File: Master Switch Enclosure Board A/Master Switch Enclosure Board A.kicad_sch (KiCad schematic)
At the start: 22 parts, among them J1 DRC Connector, J10 2-pin Microfit, J11 2-pin Microfit, J12 1-pin Microfit, J13 2-pin Microfit, J2 DTM Connector, J3 XT90, J4 XT90, J5 Screw_Terminal_01x05, J5 XT90, J6 XT90, J7 2-pin Microfit, J8 4-pin Microfit, J9 2-pin Microfit, J9 DB9_Female

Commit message: schematics ready for review
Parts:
- J2: value DTM Connector -> Ribbon Connector
- JP1: footprint (none) -> Jumper:SolderJumper-2_P1.3mm_Open_RoundedPad1.0x1.5mm
- renumbered D1 to D11, J5 to J14, J9 to J15, R1 to R11, R2 to R12, R3 to R13, R4 to R14
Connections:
- net CANH_e is gone; now on net CANH_EM: J8.4 (Pin_4)
- net CANL_e is gone; now on net CANL_EM: J8.3 (Pin_3)
- net VCU_out is gone; now on net VCUWake_out: J11.2 (Pin_2)
- net GND: now also J2.20 (Pin_20)
- no-connect marks 8 -> 7

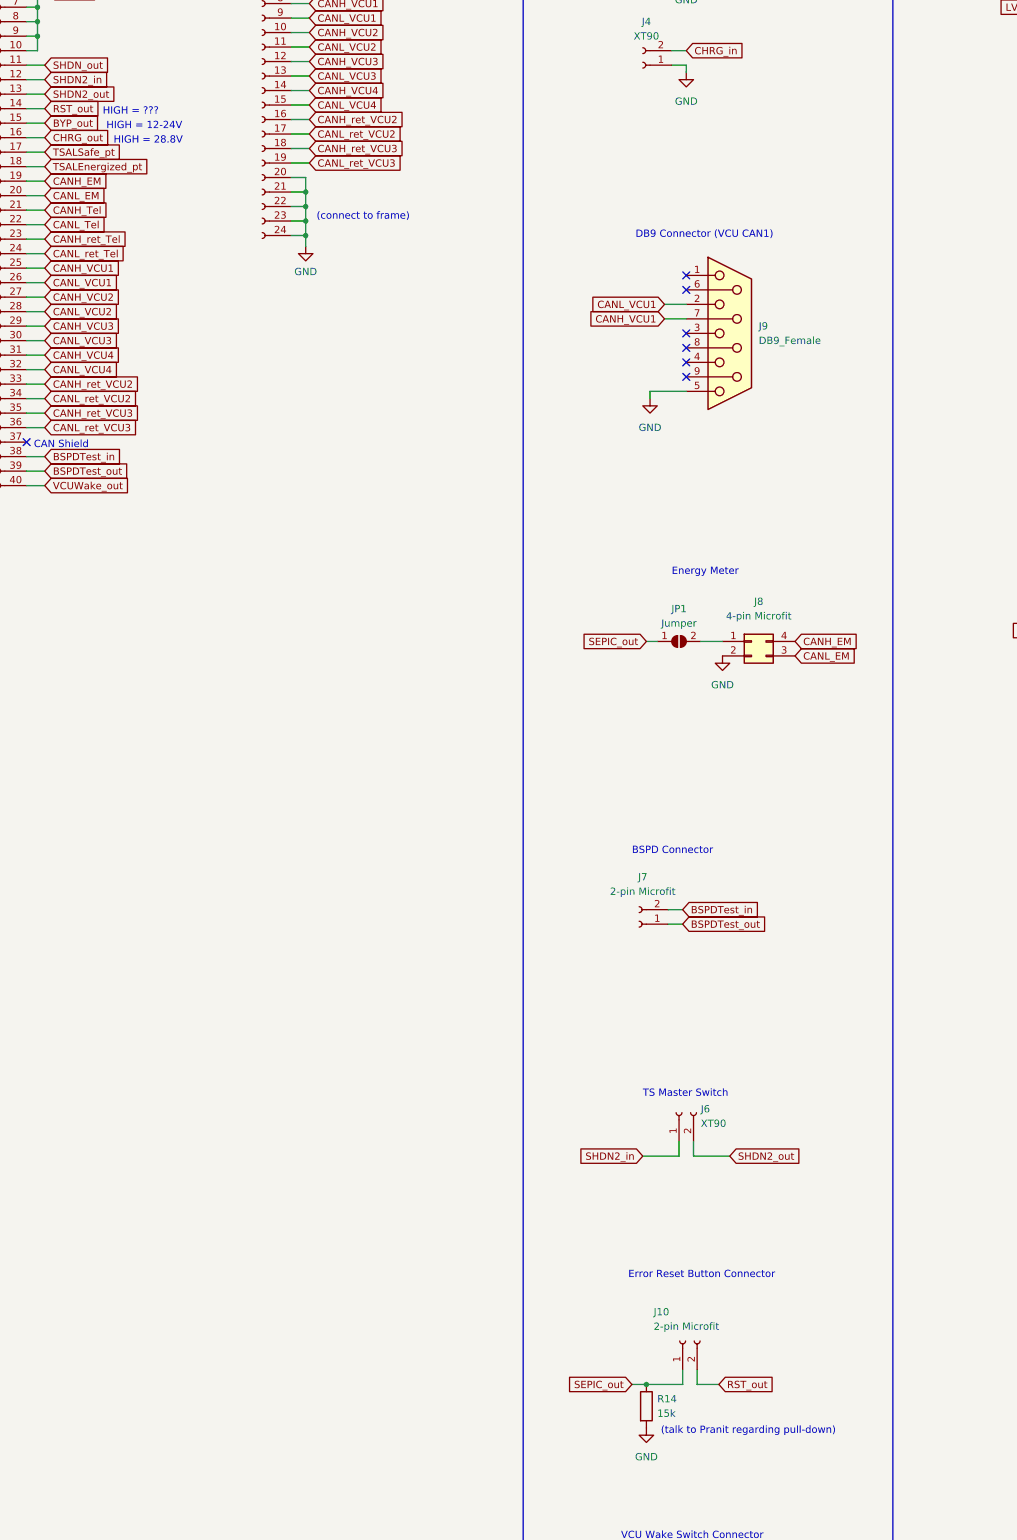
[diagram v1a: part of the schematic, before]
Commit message: resolved error reset requirements
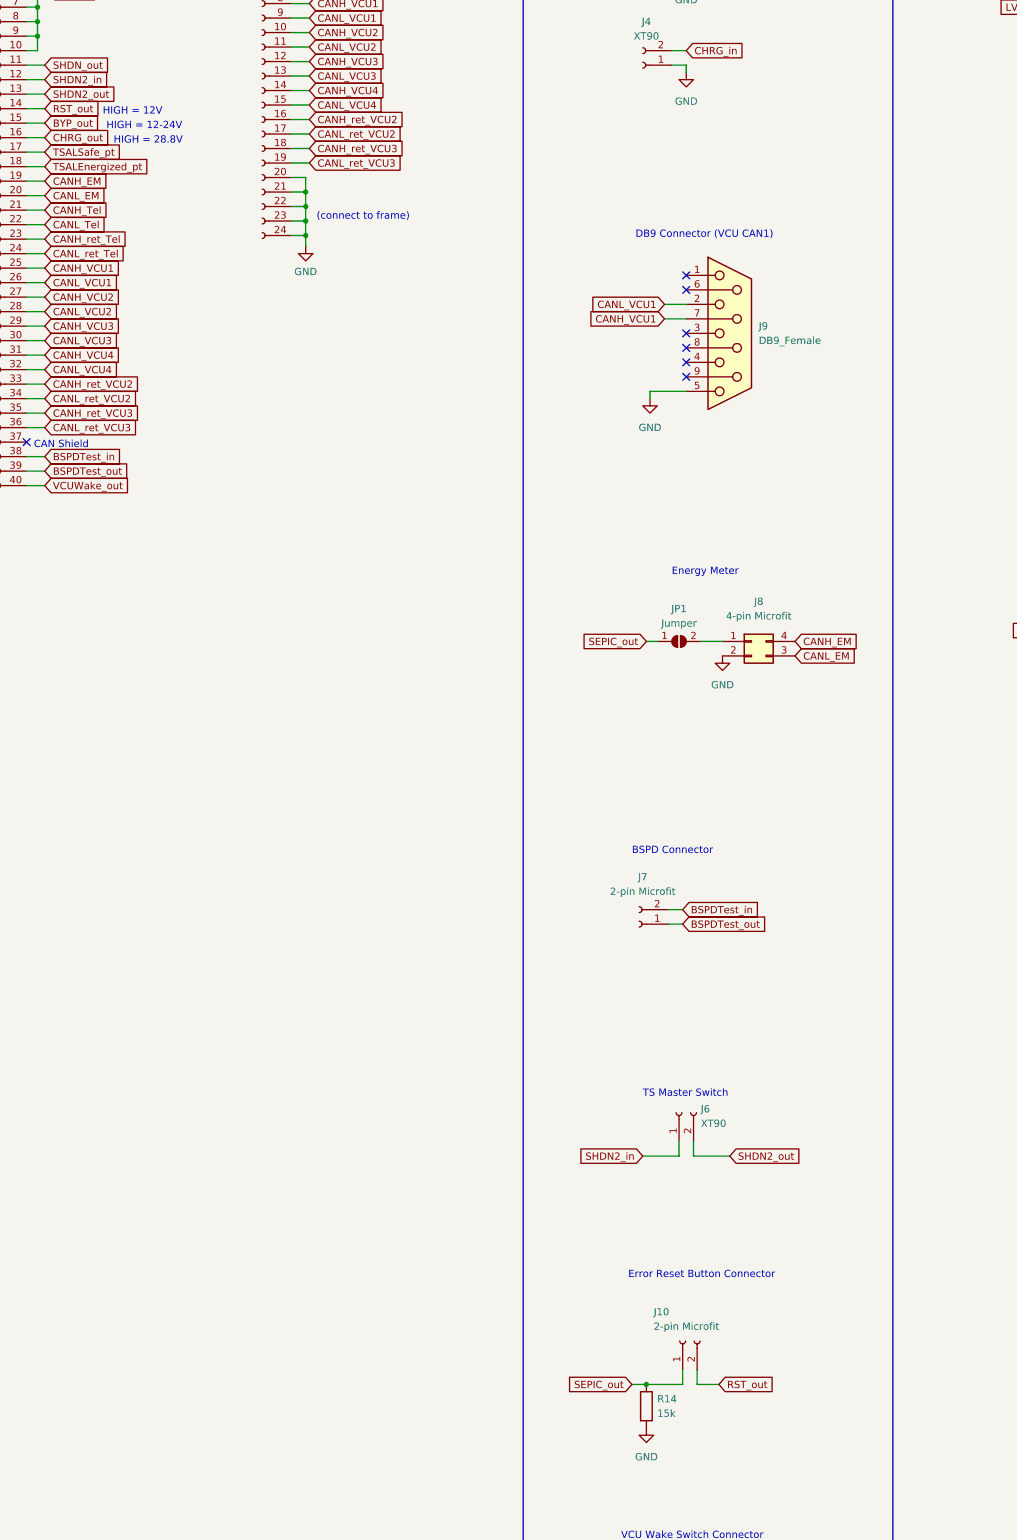
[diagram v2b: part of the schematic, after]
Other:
- note added: "HIGH = 12V"
- note removed: "(talk to Pranit regarding pull-down)"
- note removed: "HIGH = ???"
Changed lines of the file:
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@@
     (effects (font (size 1.27 1.27)) (justify left bottom))
   )
-  (text "HIGH = ???" (at 52.705 85.725 0)
+  (text "HIGH = 12V" (at 52.705 85.725 0)
     (effects (font (size 1.27 1.27)) (justify left bottom))
   )
@@
     (effects (font (size 3 3)) (justify left bottom))
   )
-  (text "(talk to Pranit regarding pull-down)" (at 150.495 316.865 0)
-    (effects (font (size 1.27 1.27)) (justify left bottom))
-  )
   (text "DB9 Connector (VCU CAN1)" (at 146.05 107.315 0)

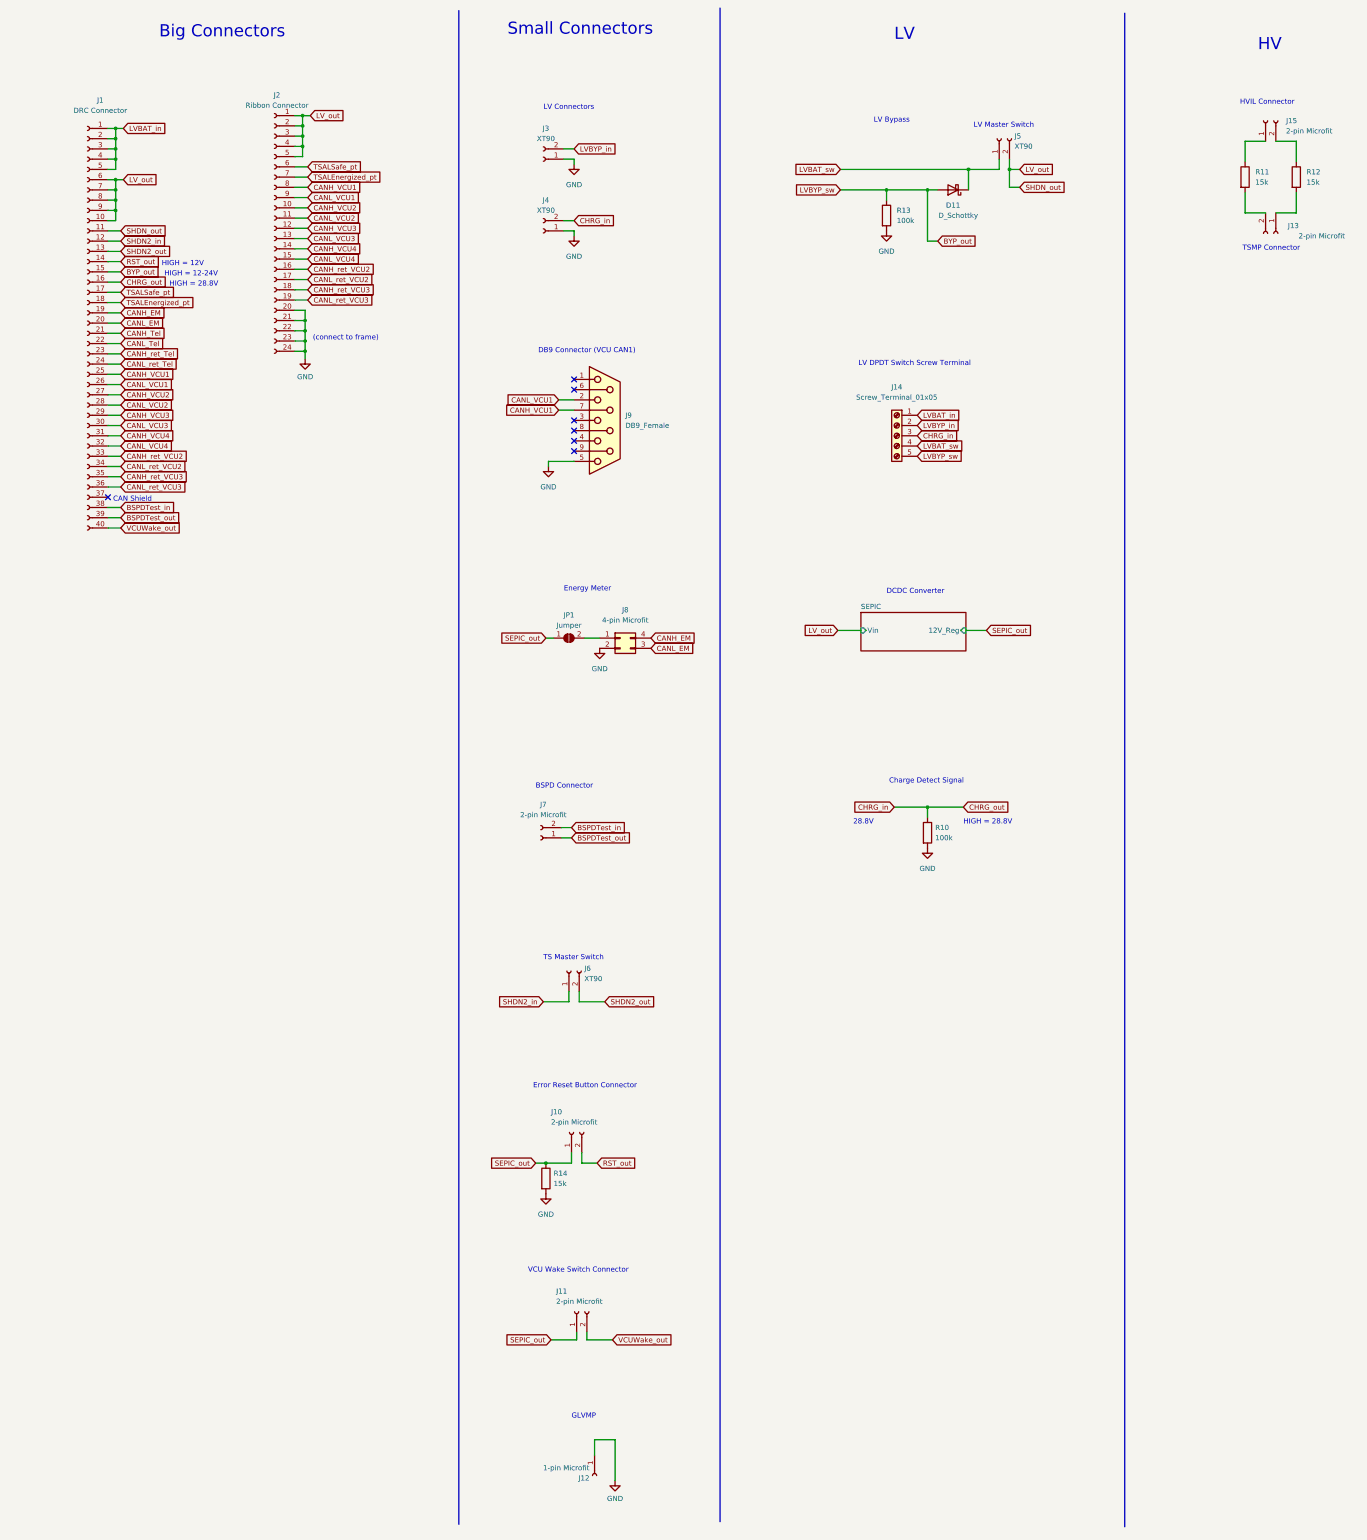
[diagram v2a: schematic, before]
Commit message: PCB partial layout
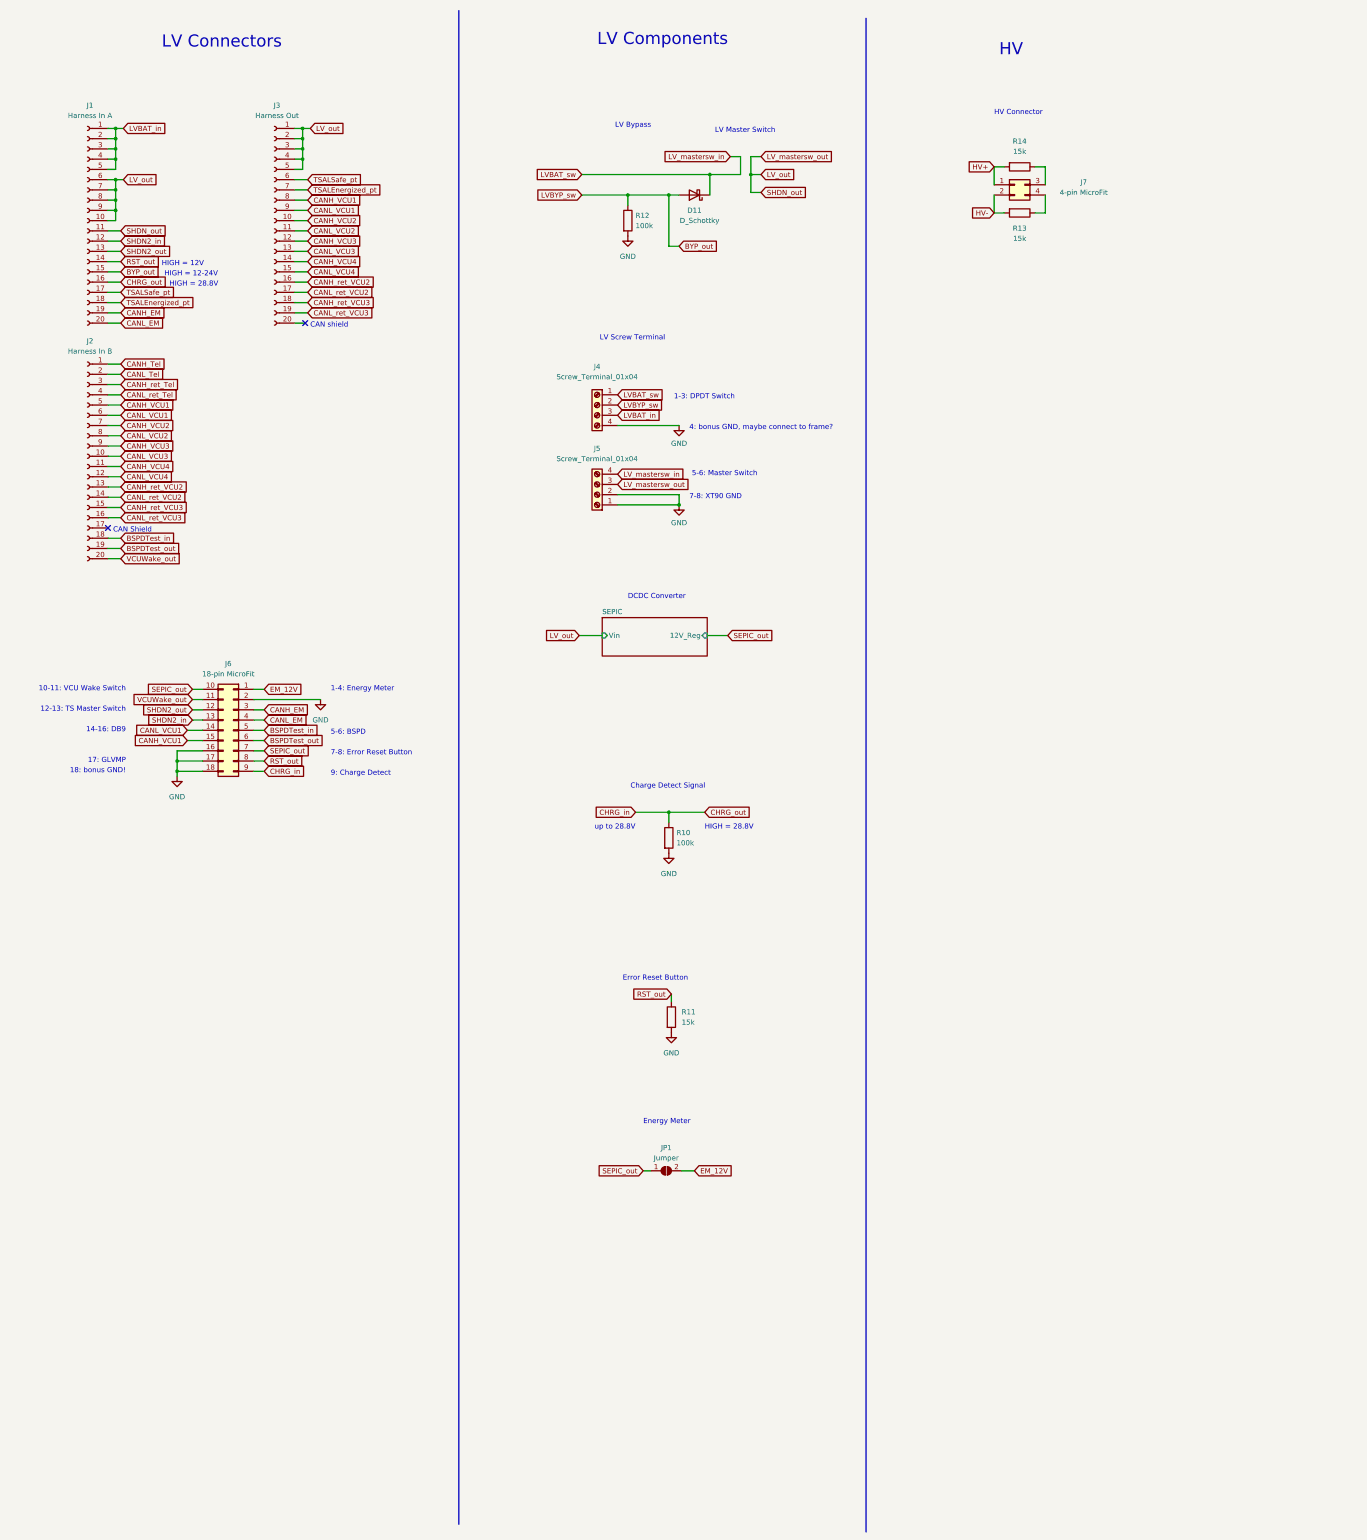
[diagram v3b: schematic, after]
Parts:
- removed J1: DRC Connector, symbol Connector:Conn_01x40_Female
- removed J10, J11, J13, J15, J7: 2-pin Microfit, symbol Connector:Conn_01x02_Female
- removed J12: 1-pin Microfit, symbol Connector:Conn_01x01_Female
- removed J14: Screw_Terminal_01x05, symbol Connector:Screw_Terminal_01x05
- removed J2: Ribbon Connector, symbol Connector:Conn_01x24_Female
- removed J3, J4, J5, J6: XT90, symbol Connector:Conn_01x02_Female
- removed J8: 4-pin Microfit, symbol Connector_Generic:Conn_02x02_Counter_Clockwise
- removed J9: DB9_Female, symbol Connector:DB9_Female
- added J1: Harness In A, Connector_Molex:Molex_Micro-Fit_3.0_43045-2012_2x10_P3.00mm_Vertical, symbol Connector:Conn_01x20_Female
- added J2: Harness In B, Connector_Molex:Molex_Micro-Fit_3.0_43045-2012_2x10_P3.00mm_Vertical, symbol Connector:Conn_01x20_Female
- added J3: Harness Out, Connector_Molex:Molex_Micro-Fit_3.0_43045-2012_2x10_P3.00mm_Vertical, symbol Connector:Conn_01x20_Female
- added J4, J5: Screw_Terminal_01x04, TerminalBlock_Phoenix:TerminalBlock_Phoenix_MKDS-3-4-5.08_1x04_P5.08mm_Horizontal, symbol Connector:Screw_Terminal_01x04
- added J6: 18-pin MicroFit, Connector_Molex:Molex_Micro-Fit_3.0_43045-1812_2x09_P3.00mm_Vertical, symbol Connector_Generic:Conn_02x09_Top_Bottom
- added J7: 4-pin MicroFit, Connector_Molex:Molex_Micro-Fit_3.0_43045-0412_2x02_P3.00mm_Vertical, symbol Connector_Generic:Conn_02x02_Top_Bottom
- D11: footprint (none) -> Global Libraries:MBRB41H100CTT4G
- R10: footprint (none) -> Resistor_SMD:R_0603_1608Metric_Pad0.98x0.95mm_HandSolder
- R11: renamed from R14; footprint (none) -> Resistor_SMD:R_0603_1608Metric_Pad0.98x0.95mm_HandSolder
- R12: renamed from R13; footprint (none) -> Resistor_SMD:R_0603_1608Metric_Pad0.98x0.95mm_HandSolder
- R13: renamed from R12; footprint (none) -> Resistor_SMD:R_0603_1608Metric_Pad0.98x0.95mm_HandSolder
- R14: renamed from R11; footprint (none) -> Resistor_SMD:R_0603_1608Metric_Pad0.98x0.95mm_HandSolder
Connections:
- net BSPDTest_in: now also J2.18 (Pin_18), J6.5 (Pin_5)
- net BSPDTest_out: now also J2.19 (Pin_19), J6.6 (Pin_6)
- net BYP_out: now also J1.15 (Pin_15), J4.2 (Pin_2)
- net CANH_EM: now also J1.19 (Pin_19), J6.3 (Pin_3)
- net CANH_Tel: now also J2.1 (Pin_1)
- net CANH_VCU1: now also J2.5 (Pin_5), J3.8 (Pin_8), J6.15 (Pin_15)
- net CANH_VCU2: now also J2.7 (Pin_7), J3.10 (Pin_10)
- net CANH_VCU3: now also J2.9 (Pin_9), J3.12 (Pin_12)
- net CANH_VCU4: now also J2.11 (Pin_11), J3.14 (Pin_14)
- net CANH_ret_Tel: now also J2.3 (Pin_3)
- net CANH_ret_VCU2: now also J2.13 (Pin_13), J3.16 (Pin_16)
- net CANH_ret_VCU3: now also J2.15 (Pin_15), J3.18 (Pin_18)
- net CANL_EM: now also J1.20 (Pin_20), J6.4 (Pin_4)
- net CANL_Tel: now also J2.2 (Pin_2)
- net CANL_VCU1: now also J2.6 (Pin_6), J3.9 (Pin_9), J6.14 (Pin_14)
- net CANL_VCU2: now also J2.8 (Pin_8), J3.11 (Pin_11)
- net CANL_VCU3: now also J2.10 (Pin_10), J3.13 (Pin_13)
- net CANL_VCU4: now also J2.12 (Pin_12), J3.15 (Pin_15)
- net CANL_ret_Tel: now also J2.4 (Pin_4)
- net CANL_ret_VCU2: now also J2.14 (Pin_14), J3.17 (Pin_17)
- net CANL_ret_VCU3: now also J2.16 (Pin_16), J3.19 (Pin_19)
- net CHRG_in: now also J1.16 (Pin_16), J6.9 (Pin_9)
- net GND: now also J4.4 (Pin_4), J5.1 (Pin_1), J5.2 (Pin_2), J6.16 (Pin_16), J6.17 (Pin_17), J6.18 (Pin_18), J6.2 (Pin_2)
- net LVBAT_in: now also J1.1 (Pin_1), J1.2 (Pin_2), J1.3 (Pin_3), J1.4 (Pin_4), J1.5 (Pin_5), J4.3 (Pin_3)
- net LVBAT_sw: now also J4.1 (Pin_1), J5.4 (Pin_4)
- net RST_out: now also R11.1, J1.14 (Pin_14), J6.8 (Pin_8)
- net SEPIC_out: now also J6.10 (Pin_10), J6.7 (Pin_7); no longer R11.1
- net SHDN2_in: now also J1.12 (Pin_12), J6.13 (Pin_13)
- net SHDN2_out: now also J1.13 (Pin_13), J6.12 (Pin_12)
- net TSALEnergized_pt: now also J1.18 (Pin_18), J3.7 (Pin_7)
- net TSALSafe_pt: now also J1.17 (Pin_17), J3.6 (Pin_6)
- net VCUWake_out: now also J2.20 (Pin_20), J6.11 (Pin_11)
- net HV-: now reaches R13.2
- net HV-: now also J7.2 (Pin_2)
- net HV+: now reaches R14.2
- net HV+: now also J7.1 (Pin_1)
- net at R14.1: now also J7.3 (Pin_3)
- net at R13.1: now also J7.4 (Pin_4)
- net EM_12V: now reaches JP1.2 (B)
- net EM_12V: now also J6.1 (Pin_1)
- new net LV_mastersw_out: J1.10 (Pin_10), J1.11 (Pin_11), J1.6 (Pin_6), J1.7 (Pin_7), J1.8 (Pin_8), J1.9 (Pin_9), J3.1 (Pin_1), J3.2 (Pin_2), J3.3 (Pin_3), J3.4 (Pin_4), J3.5 (Pin_5), J5.3 (Pin_3)
- no-connect marks 7 -> 2
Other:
- note added: "1-3: DPDT Switch"
- note added: "1-4: Energy Meter"
- note added: "10-11: VCU Wake Switch"
- note added: "12-13: TS Master Switch"
- note added: "14-16: DB9"
- note added: "17: GLVMP"
- note added: "18: bonus GND!"
- note added: "4: bonus GND, maybe connect to frame?"
- note added: "5-6: BSPD"
- note added: "5-6: Master Switch"
- note added: "7-8: Error Reset Button"
- note added: "7-8: XT90 GND"
- note added: "9: Charge Detect"
- note added: "CAN shield"
- note added: "Error Reset Button"
- note added: "HV Connector"
- note added: "LV Components"
- note added: "LV Screw Terminal"
- note added: "up to 28.8V"
- note removed: "(connect to frame)"
- note removed: "28.8V"
- note removed: "BSPD Connector"
- note removed: "Big Connectors"
- note removed: "DB9 Connector (VCU CAN1)"
- note removed: "Error Reset Button Connector"
- note removed: "GLVMP"
- note removed: "HVIL Connector"
- note removed: "LV"
- note removed: "LV DPDT Switch Screw Terminal"
- note removed: "Small Connectors"
- note removed: "TS Master Switch"
- note removed: "TSMP Connector"
- note removed: "VCU Wake Switch Connector"
- moved on the sheet: D11, JP1, R10, R11, R12, R13, R14
